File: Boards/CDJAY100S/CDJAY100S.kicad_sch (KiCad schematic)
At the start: 70 parts, among them CN701 52492-3620, CN705 52151-1410, J1 Rotary Encoder, U1 PT6324Q, U2 TXS0108EPW

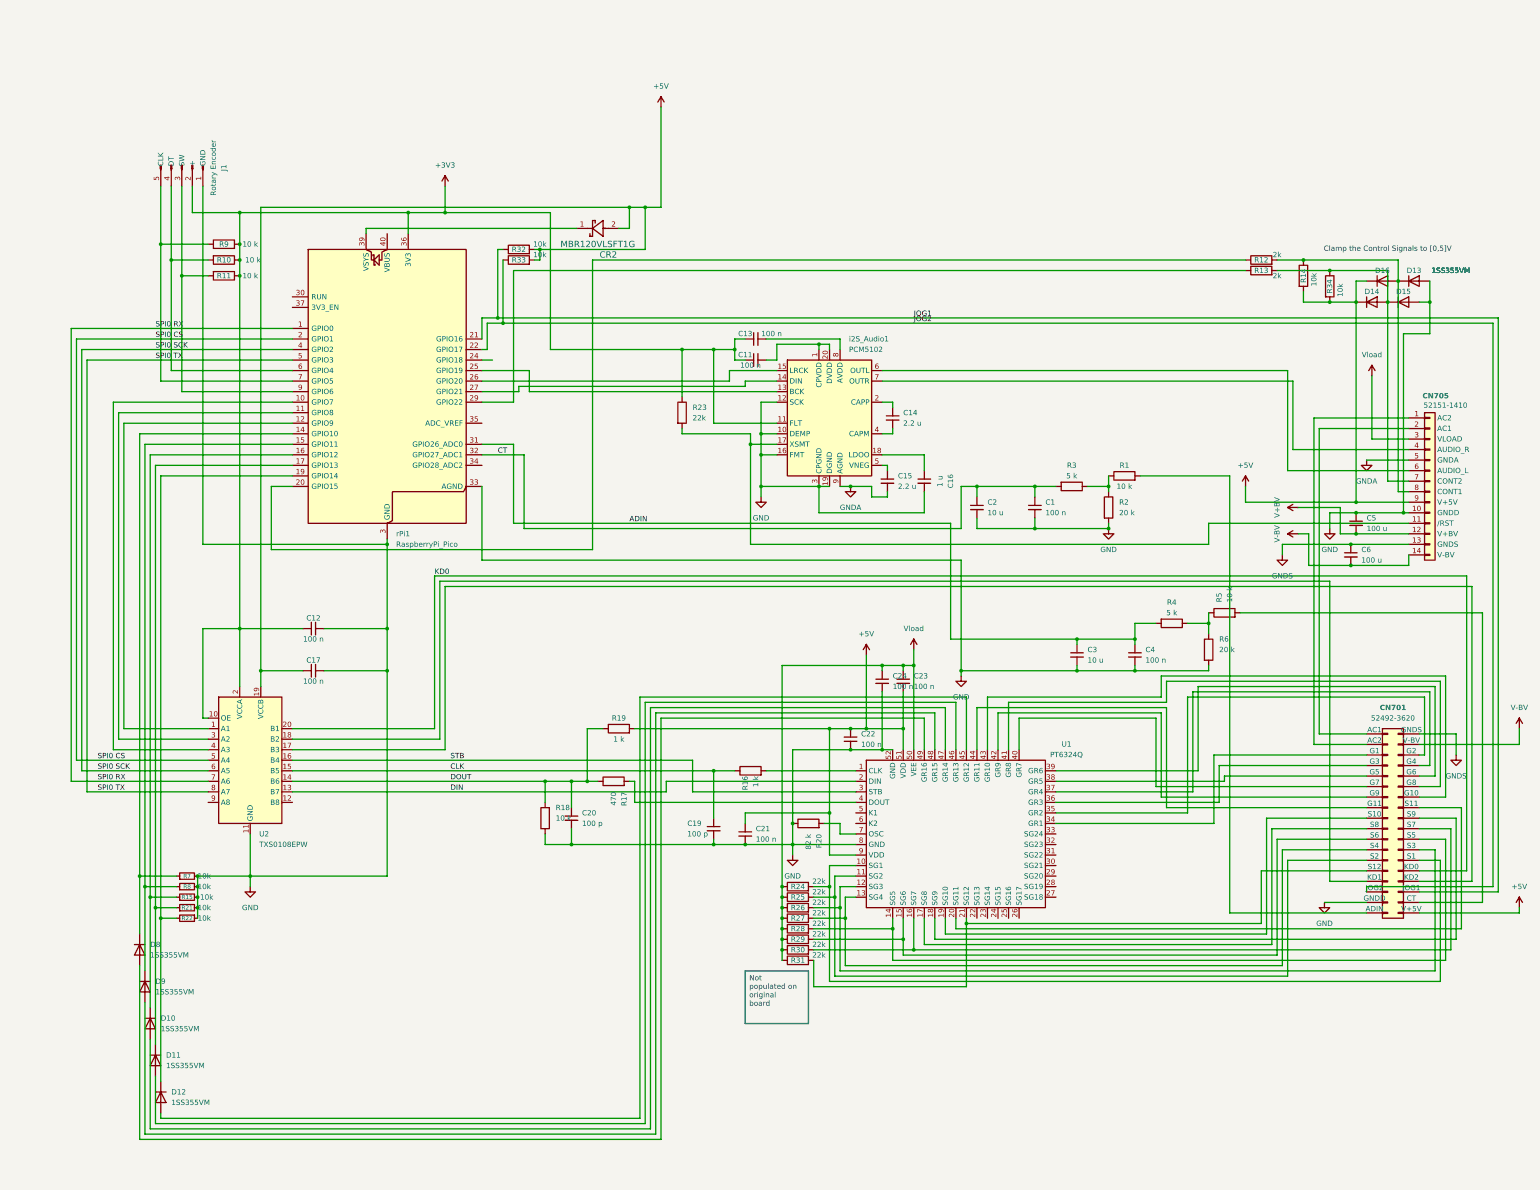
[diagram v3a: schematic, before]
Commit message: Include USB-Hub
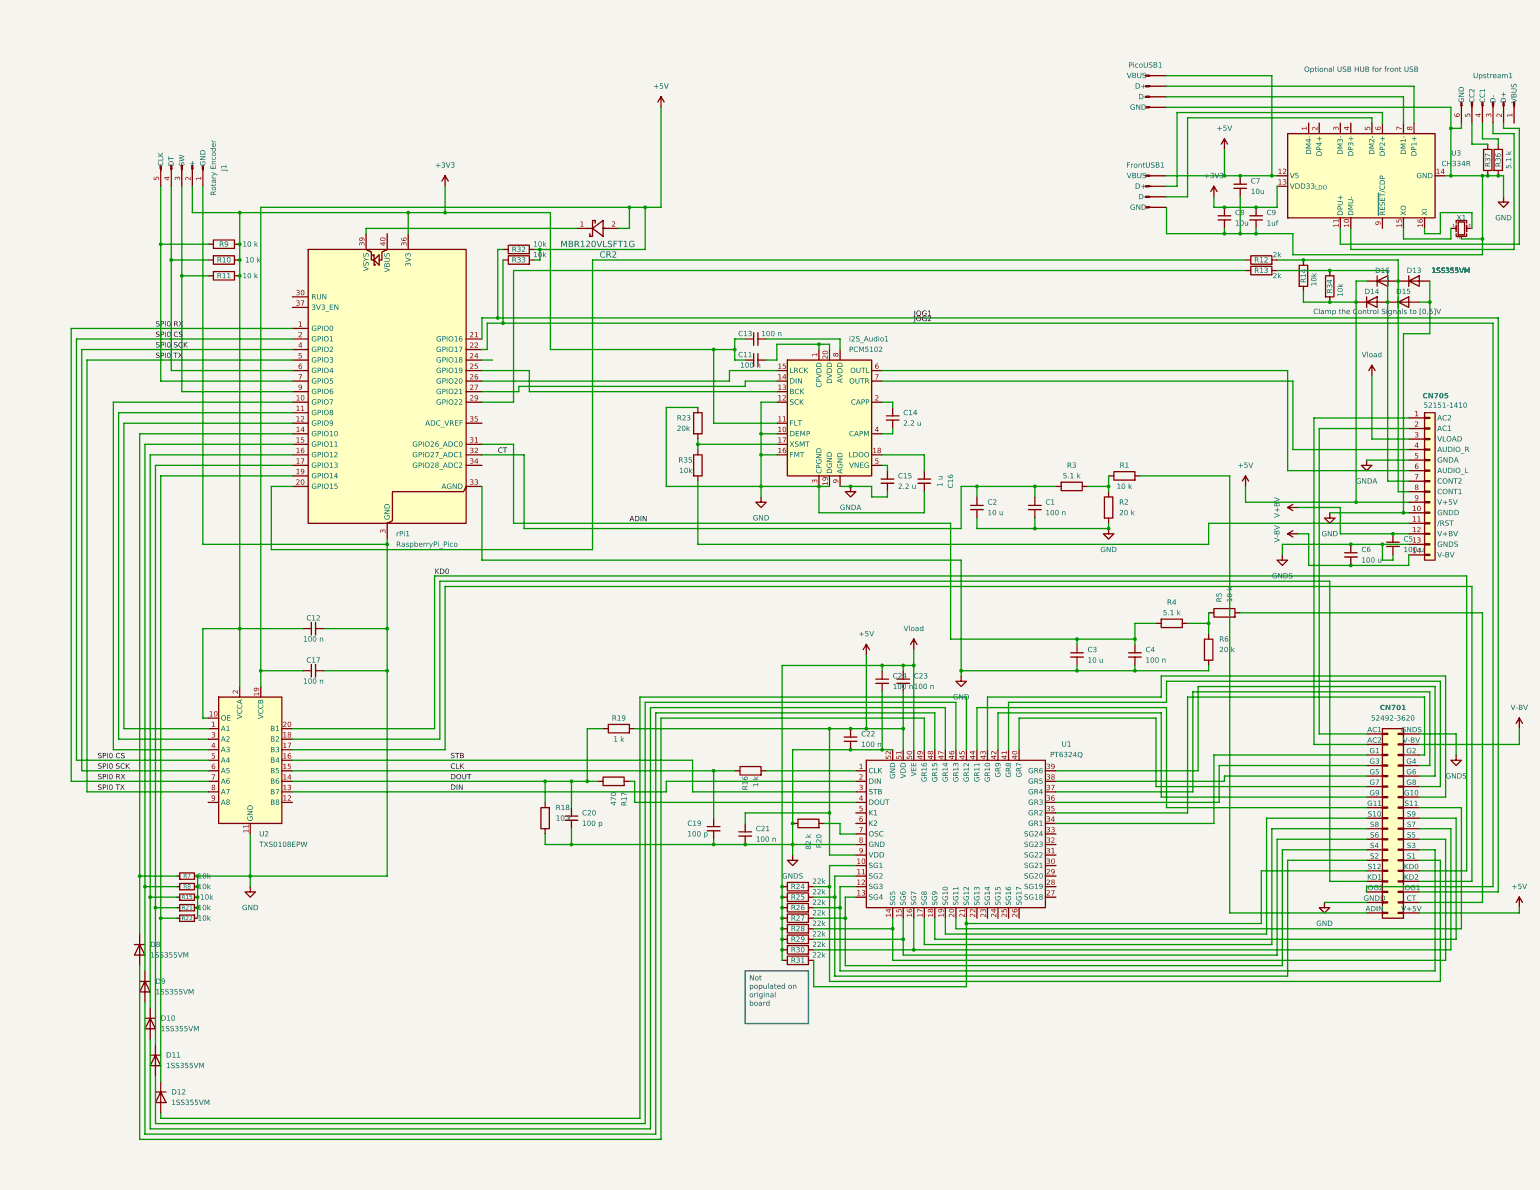
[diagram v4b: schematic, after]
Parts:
- added C7, C8: 10u, Capacitor_SMD:C_1206_3216Metric_Pad1.33x1.80mm_HandSolder, symbol Device:C_Small
- added C9: 1uf, Capacitor_SMD:C_1206_3216Metric_Pad1.33x1.80mm_HandSolder, symbol Device:C_Small
- added FrontUSB1, PicoUSB1: Conn_01x04_Pin, Connector_PinHeader_2.54mm:PinHeader_1x04_P2.54mm_Vertical, symbol Connector:Conn_01x04_Pin
- added R35: 10k, Resistor_SMD:R_1206_3216Metric_Pad1.30x1.75mm_HandSolder, symbol Device:R
- added R36, R37: 5.1 k, Resistor_SMD:R_1206_3216Metric_Pad1.30x1.75mm_HandSolder, symbol Device:R
- added U3: CH334R, Package_SO:QSOP-16_3.9x4.9mm_P0.635mm, symbol Interface_USB:CH334R
- added Upstream1: Conn_01x06_Pin, Connector_PinHeader_2.54mm:PinHeader_1x06_P2.54mm_Vertical, symbol Connector:Conn_01x06_Pin
- added X1: 12MHz, Crystal:Crystal_SMD_3225-4Pin_3.2x2.5mm_HandSoldering, symbol Device:Crystal_GND24_Small
- R23: value 22k -> 20k
- R3, R4: value 5 k -> 5.1 k
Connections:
- net +3V3: now also C8.1, C9.1, U3.13 (VDD33_{LDO}); no longer R23.1
- net +5V: now also C7.1, FrontUSB1.1 (VBUS), PicoUSB1.1 (VBUS), U3.12 (V5)
- net GND: now also R23.1, C7.2, C8.2, C9.2, FrontUSB1.4 (GND), PicoUSB1.4 (GND), R36.2, R37.2, U3.14 (GND), Upstream1.6 (GND), X1.2 (G), X1.4 (G); no longer C19.2, C20.2, C21.2, C22.2, C24.2, C5.1, R18.1, R20.1, U1.52 (GND), U1.8 (GND)
- net GNDS: now also C19.2, C20.2, C21.2, C22.2, C24.2, C5.2, R18.1, R20.1, U1.52 (GND), U1.8 (GND)
- net V+BV: now also C5.1; no longer C5.2
- net at R23.2, i2S_Audio1.17 (XSMT): now also R35.1; no longer CN705.11 (/RST)
- new net: U3.10 (DMU-), Upstream1.3 (D-)
- new net: U3.11 (DPU+), Upstream1.2 (D+)
- new net: U3.15 (XO), X1.1
- new net: U3.16 (XI), X1.3
- new net: FrontUSB1.3 (D-), U3.5 (DM2-)
- new net: FrontUSB1.2 (D+), U3.6 (DP2+)
- new net: PicoUSB1.3 (D-), U3.7 (DM1-)
- new net: PicoUSB1.2 (D+), U3.8 (DP1+)
- new net: R37.1, Upstream1.5 (CC2)
- new net: R36.1, Upstream1.4 (CC1)
- new net: CN705.11 (/RST), R35.2
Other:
- note added: "Optional USB HUB for front USB"
- moved on the sheet: C5, R23

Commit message: Board Revision 1.4
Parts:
- removed C20: 100 p, Capacitor_SMD:C_1206_3216Metric_Pad1.33x1.80mm_HandSolder, symbol Device:C_Small
- removed R17: 470, Resistor_SMD:R_1206_3216Metric_Pad1.30x1.75mm_HandSolder, symbol Device:R
- removed R18: 10 k, Resistor_SMD:R_1206_3216Metric_Pad1.30x1.75mm_HandSolder, symbol Device:R
- removed R19: 1 k, Resistor_SMD:R_1206_3216Metric_Pad1.30x1.75mm_HandSolder, symbol Device:R
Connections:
- net at D9.2 (A): now also U1.46 (GR13); no longer U1.48 (GR15)
- net at D11.2 (A): now also U1.48 (GR15); no longer U1.46 (GR13)
- net at U1.45 (GR12): now also D8.2 (A); no longer D12.2 (A)
- net at U1.49 (GR16): now also D12.2 (A); no longer D8.2 (A)
- net DOUT: no longer names the net of U2.14 (B6)

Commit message: Board Revision 1.5
Only cosmetic changes
- Fixed the footprint of the 36p connector to remove the bottom screen covering the copper
- Added a solder jumper to connect the /rst pin to the pico if needed
- moved MH3 down 0.5mm
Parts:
- added JP1: SolderJumper_2_Open, Jumper:SolderJumper-2_P1.3mm_Open_Pad1.0x1.5mm, symbol Jumper:SolderJumper_2_Open
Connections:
- net at R23.2, R35.1, i2S_Audio1.17 (XSMT): now also JP1.2 (B)
- net at rPi1.37 (3V3_EN): now also JP1.1 (A)
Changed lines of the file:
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@@
 	(title_block
 		(title "CDJay 100 Mainboard")
-		(date "2026-09-01")
-		(rev "1.2")
+		(date "2026-09-15")
+		(rev "1.5")
 		(company "FH Aachen University of Applied Sciences")
 		(comment 1 "applab.fh-aachen.de")
@@
 	)
 	(junction
+		(at 209.55 105.41)
+		(diameter 0)
+		(color 0 0 0 0)
+	)
+	(junction
 		(at 248.92 179.07)
 		(diameter 0)
@@
 	(wire
 		(pts
+			(xy 209.55 105.41) (xy 223.52 105.41)
+		)
+		(stroke
+			(width 0)
+			(type default)
+		)
+	)
+	(wire
+		(pts
 			(xy 353.06 99.06) (xy 353.06 177.8)
 		)
@@
 	(wire
 		(pts
+			(xy 116.84 50.8) (xy 209.55 50.8)
+		)
+		(stroke
+			(width 0)
+			(type default)
+		)
+	)
+	(wire
+		(pts
 			(xy 208.28 201.93) (xy 215.9 201.93)
 		)
@@
 	(wire
 		(pts
+			(xy 102.87 50.8) (xy 106.68 50.8)
+		)
+		(stroke
+			(width 0)
+			(type default)
+		)
+	)
+	(wire
+		(pts
 			(xy 290.83 184.15) (xy 325.12 184.15)
 		)
@@
 	(wire
 		(pts
-			(xy 204.47 105.41) (xy 223.52 105.41)
+			(xy 204.47 105.41) (xy 209.55 105.41)
 		)
 		(stroke
@@
 	(wire
 		(pts
+			(xy 209.55 50.8) (xy 209.55 105.41)
+		)
+		(stroke
+			(width 0)
+			(type default)
+		)
+	)
+	(wire
+		(pts
 			(xy 129.54 149.86) (xy 129.54 160.02)
 		)
@@
 	(wire
 		(pts
+			(xy 102.87 72.39) (xy 102.87 50.8)
+		)
+		(stroke
+			(width 0)
+			(type default)
+		)
+	)
+	(wire
+		(pts
 			(xy 195.58 171.45) (xy 195.58 273.05)
 		)
@@
 	(wire
 		(pts
+			(xy 106.68 72.39) (xy 102.87 72.39)
+		)
+		(stroke
+			(width 0)
+			(type default)
+		)
+	)
+	(wire
+		(pts
 			(xy 347.98 54.61) (xy 347.98 59.69)
 		)
@@
 					(unit 1)
 				)
+			)
+		)
+	)
+	(symbol
+		(lib_id "Jumper:SolderJumper_2_Open")
+		(at 111.76 50.8 0)
+		(unit 1)
+		(body_style 1)
+		(exclude_from_sim no)
+		(in_bom no)
+		(on_board yes)
+		(in_pos_files yes)
+		(dnp no)
+		(fields_autoplaced yes)
+		(property "Reference" "JP1"
+			(at 111.76 46.99 0)
+			(show_name no)
+			(do_not_autoplace no)
+			(effects
+				(font
+					(size 1.27 1.27)
+				)
+			)
+		)
+		(property "Value" "SolderJumper_2_Open"
+			(at 111.76 46.99 0)
+			(hide yes)
+			(show_name no)
+			(do_not_autoplace no)
+			(effects
+				(font
+					(size 1.27 1.27)
+				)
+			)
+		)
+		(property "Footprint" "Jumper:SolderJumper-2_P1.3mm_Open_Pad1.0x1.5mm"
+			(at 111.76 50.8 0)
+			(hide yes)
+			(show_name no)
+			(do_not_autoplace no)
+			(effects
+				(font
+					(size 1.27 1.27)
+				)
+			)
+		)
+		(property "Datasheet" ""
+			(at 111.76 58.42 0)
+			(hide yes)
+			(show_name no)
+			(do_not_autoplace no)
+			(effects
+				(font
+					(size 1.27 1.27)
+				)
+			)
+		)
+		(property "Description" "Solder Jumper, 2-pole, open"
+			(at 111.76 55.88 0)
+			(hide yes)
+			(show_name no)
+			(do_not_autoplace no)
+			(effects
+				(font
+					(size 1.27 1.27)
+				)
+			)
+		)
+		(pin "2"
+		)
+		(pin "1"
+		)
+		(instances
+			(project "CDJAY100S"
+				(path "/7da26f59-1cc1-4d8c-b6c1-66e5f20ab1d6"
+					(reference "JP1")
+					(unit 1)
+				)
